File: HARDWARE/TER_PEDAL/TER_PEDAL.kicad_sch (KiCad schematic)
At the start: 6 parts

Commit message: Sized and Fixed even more footprints + Initial layout
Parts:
- R13, R14: footprint Resistor_SMD:R_0603_1608Metric -> Resistor_SMD:R_0402_1005Metric
- R15: footprint Capacitor_SMD:C_0603_1608Metric -> Capacitor_SMD:C_0402_1005Metric
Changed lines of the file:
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@@
       (effects (font (size 1.27 1.27)))
     )
-    (property "Footprint" "Resistor_SMD:R_0603_1608Metric" (at 38.1 170.688 90)
+    (property "Footprint" "Resistor_SMD:R_0402_1005Metric" (at 38.1 170.688 90)
       (effects (font (size 1.27 1.27)) hide)
     )
@@
       (effects (font (size 1.27 1.27)))
     )
-    (property "Footprint" "Capacitor_SMD:C_0603_1608Metric" (at 38.1 184.658 90)
+    (property "Footprint" "Capacitor_SMD:C_0402_1005Metric" (at 38.1 184.658 90)
       (effects (font (size 1.27 1.27)) hide)
     )
@@
       (effects (font (size 1.27 1.27)))
     )
-    (property "Footprint" "Resistor_SMD:R_0603_1608Metric" (at 38.1 165.608 90)
+    (property "Footprint" "Resistor_SMD:R_0402_1005Metric" (at 38.1 165.608 90)
       (effects (font (size 1.27 1.27)) hide)
     )

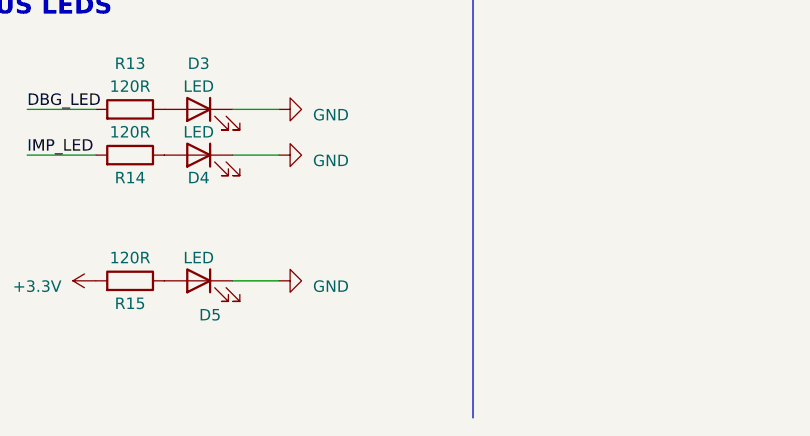
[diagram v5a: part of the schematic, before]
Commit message: Began layout and switched to 4 layer board
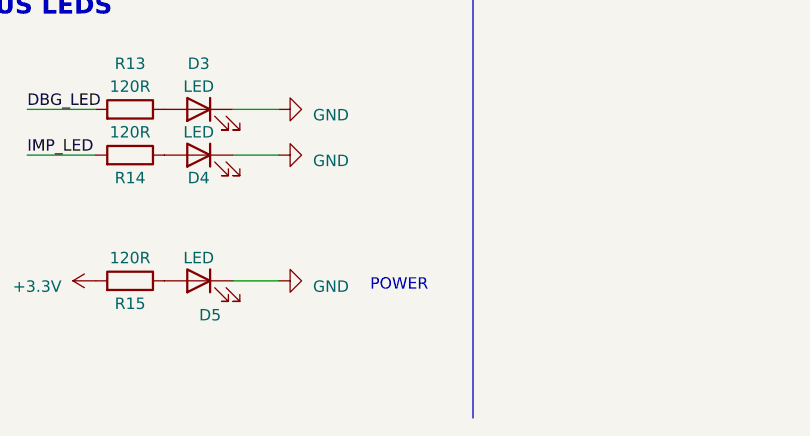
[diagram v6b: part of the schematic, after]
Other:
- note added: "POWER"
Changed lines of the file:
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@@
     (effects (font (size 2 2) (thickness 0.4) bold) (justify left bottom))
+  )
+  (text "POWER" (at 64.77 184.15 0)
+    (effects (font (size 1.27 1.27)) (justify left bottom))
   )
   (label "IMP_LED" (at 161.29 91.44 180) (fields_autoplaced)

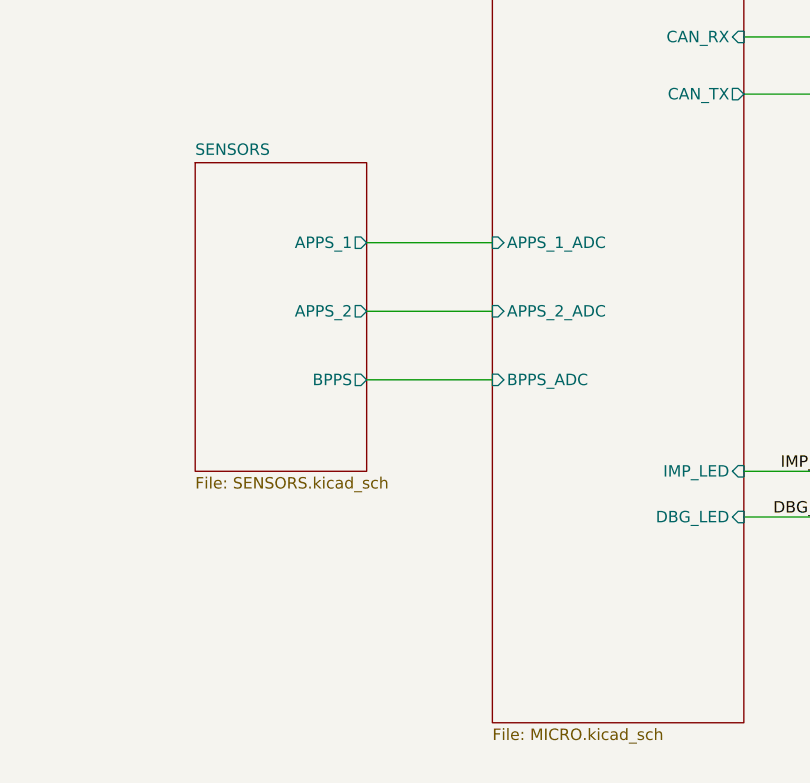
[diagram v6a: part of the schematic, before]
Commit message: Added decouple to all sensors and a new steering sensor input
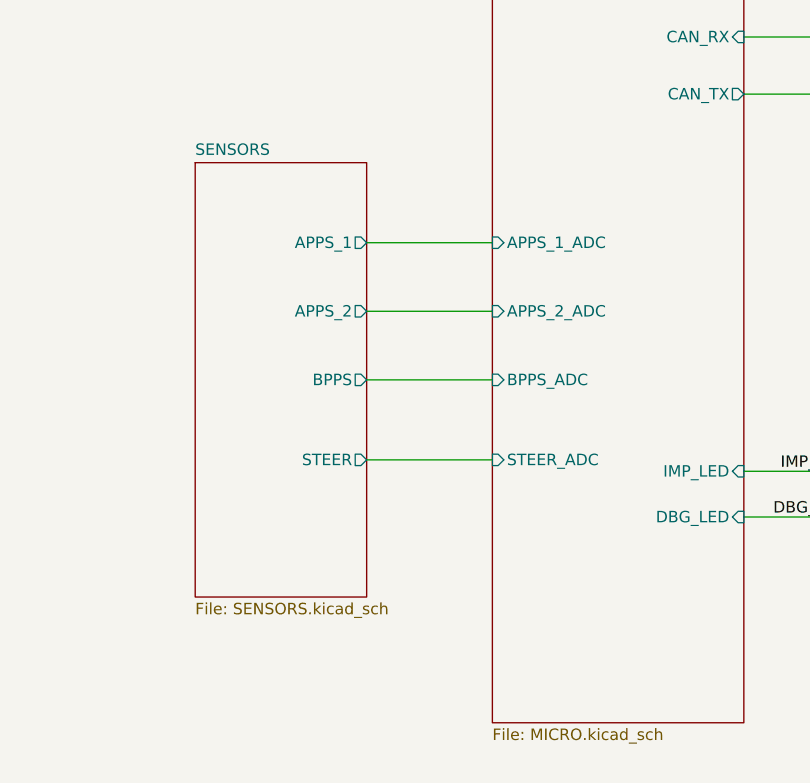
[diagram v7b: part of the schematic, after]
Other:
- sheet MICRO ports: added STEER_ADC; removed none
- sheet SENSORS ports: added STEER; removed none
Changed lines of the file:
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@@
+    (stroke (width 0) (type default))
+  )
+  (wire (pts (xy 107.95 90.17) (xy 121.92 90.17))
     (stroke (width 0) (type default))
   )
@@
       (effects (font (size 1.27 1.27)) (justify left))
     )
+    (pin "STEER_ADC" input (at 121.92 90.17 180)
+      (effects (font (size 1.27 1.27)) (justify left))
+    )
     (instances
       (project "TER_PEDAL"
@@
     )
   )
-  (sheet (at 88.9 57.15) (size 19.05 34.29) (fields_autoplaced)
+  (sheet (at 88.9 57.15) (size 19.05 48.26) (fields_autoplaced)
     (stroke (width 0.1524) (type solid))
     (fill (color 0 0 0 0.0000))
@@
       (effects (font (size 1.27 1.27)) (justify left bottom))
     )
-    (property "Sheetfile" "SENSORS.kicad_sch" (at 88.9 92.0246 0)
+    (property "Sheetfile" "SENSORS.kicad_sch" (at 88.9 105.9946 0)
       (effects (font (size 1.27 1.27)) (justify left top))
     )
@@
       (effects (font (size 1.27 1.27)) (justify right))
     )
+    (pin "STEER" output (at 107.95 90.17 0)
+      (effects (font (size 1.27 1.27)) (justify right))
+    )

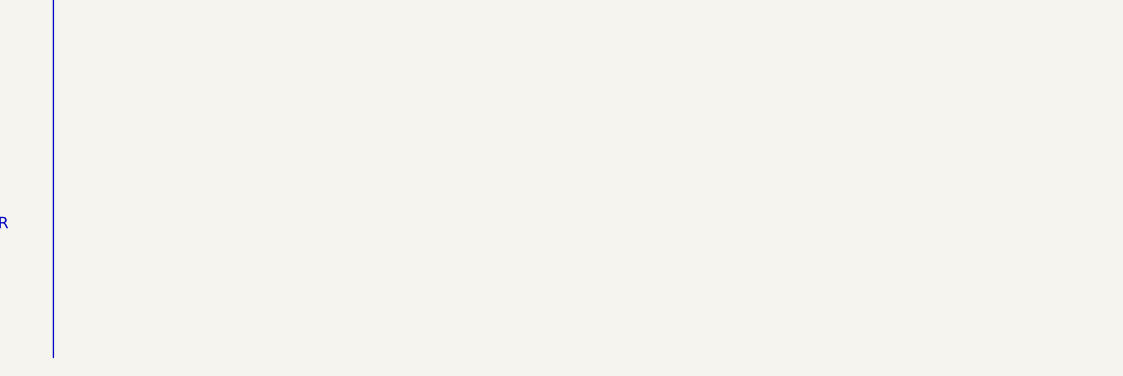
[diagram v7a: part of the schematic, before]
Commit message: Added holes, connectors and finished re-layout
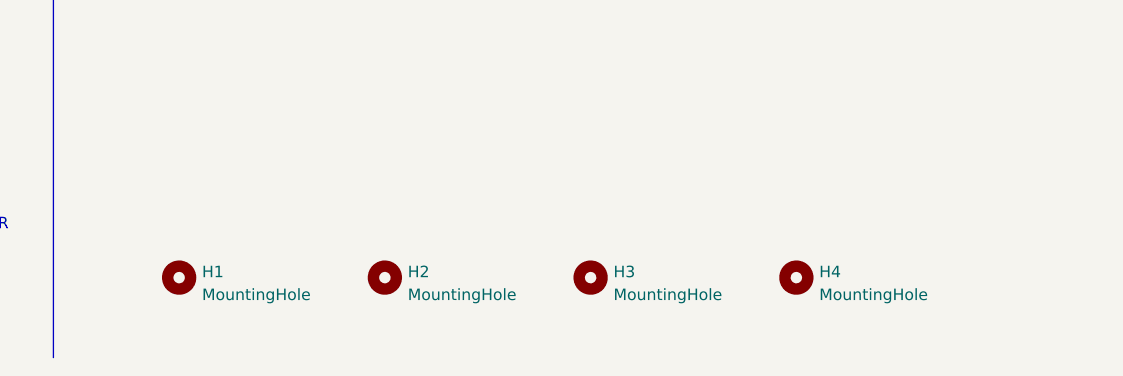
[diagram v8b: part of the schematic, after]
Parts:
- added H1, H2, H3, H4: MountingHole, MountingHole:MountingHole_2.2mm_M2, symbol Mechanical:MountingHole
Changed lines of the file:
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@@
+    )
+  )
+  (symbol (lib_id "Mechanical:MountingHole") (at 135.89 189.23 0) (unit 1)
+    (in_bom yes) (on_board yes) (dnp no) (fields_autoplaced)
+    (property "Reference" "H3" (at 138.43 188.595 0)
+      (effects (font (size 1.27 1.27)) (justify left))
+    )
+    (property "Value" "MountingHole" (at 138.43 191.135 0)
+      (effects (font (size 1.27 1.27)) (justify left))
+    )
+    (property "Footprint" "MountingHole:MountingHole_2.2mm_M2" (at 135.89 189.23 0)
+      (effects (font (size 1.27 1.27)) hide)
+    )
+    (property "Datasheet" "~" (at 135.89 189.23 0)
+      (effects (font (size 1.27 1.27)) hide)
+    )
+    (instances
+      (project "TER_PEDAL"
+        (path "/73ede3a3-6344-40fe-9207-10ff50d388ba"
+          (reference "H3") (unit 1)
+        )
+      )
+    )
+  )
+  (symbol (lib_id "Mechanical:MountingHole") (at 113.03 189.23 0) (unit 1)
+    (in_bom yes) (on_board yes) (dnp no) (fields_autoplaced)
+    (property "Reference" "H2" (at 115.57 188.595 0)
+      (effects (font (size 1.27 1.27)) (justify left))
+    )
+    (property "Value" "MountingHole" (at 115.57 191.135 0)
+      (effects (font (size 1.27 1.27)) (justify left))
+    )
+    (property "Footprint" "MountingHole:MountingHole_2.2mm_M2" (at 113.03 189.23 0)
+      (effects (font (size 1.27 1.27)) hide)
+    )
+    (property "Datasheet" "~" (at 113.03 189.23 0)
+      (effects (font (size 1.27 1.27)) hide)
+    )
+    (instances
+      (project "TER_PEDAL"
+        (path "/73ede3a3-6344-40fe-9207-10ff50d388ba"
+          (reference "H2") (unit 1)
+        )
+      )
     )
   )
@@
     )
   )
+  (symbol (lib_id "Mechanical:MountingHole") (at 158.75 189.23 0) (unit 1)
+    (in_bom yes) (on_board yes) (dnp no) (fields_autoplaced)
+    (property "Reference" "H4" (at 161.29 188.595 0)
+      (effects (font (size 1.27 1.27)) (justify left))
+    )
+    (property "Value" "MountingHole" (at 161.29 191.135 0)
+      (effects (font (size 1.27 1.27)) (justify left))
+    )
+    (property "Footprint" "MountingHole:MountingHole_2.2mm_M2" (at 158.75 189.23 0)
+      (effects (font (size 1.27 1.27)) hide)
+    )
+    (property "Datasheet" "~" (at 158.75 189.23 0)
+      (effects (font (size 1.27 1.27)) hide)
+    )
+    (instances
+      (project "TER_PEDAL"
+        (path "/73ede3a3-6344-40fe-9207-10ff50d388ba"
+          (reference "H4") (unit 1)
+        )
+      )
+    )
+  )
   (symbol (lib_id "power:+3.3V") (at 34.29 182.88 90) (unit 1)
     (in_bom yes) (on_board yes) (dnp no) (fields_autoplaced)
@@
         )
       )
+    )
+  )
+  (symbol (lib_id "Mechanical:MountingHole") (at 90.17 189.23 0) (unit 1)
+    (in_bom yes) (on_board yes) (dnp no) (fields_autoplaced)
+    (property "Reference" "H1" (at 92.71 188.595 0)
+      (effects (font (size 1.27 1.27)) (justify left))
+    )
+    (property "Value" "MountingHole" (at 92.71 191.135 0)
+      (effects (font (size 1.27 1.27)) (justify left))
+    )
+    (property "Footprint" "MountingHole:MountingHole_2.2mm_M2" (at 90.17 189.23 0)
+      (effects (font (size 1.27 1.27)) hide)
+    )
+    (property "Datasheet" "~" (at 90.17 189.23 0)
+      (effects (font (size 1.27 1.27)) hide)
+    )
+    (instances
+      (project "TER_PEDAL"
+        (path "/73ede3a3-6344-40fe-9207-10ff50d388ba"
+          (reference "H1") (unit 1)
+        )
+      )
